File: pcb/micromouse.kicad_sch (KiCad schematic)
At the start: 15 parts, among them J1 AVR-ISP-6, U1 TSSP77038ETR, U2 TSSP77038ETR, U3 TSSP77038ETR, U4 TSSP77038ETR, U5 TSSP77038ETR, U6 TSSP77038ETR, U7 ATmega328PB-A, U8 MX1508, Y1 Crystal

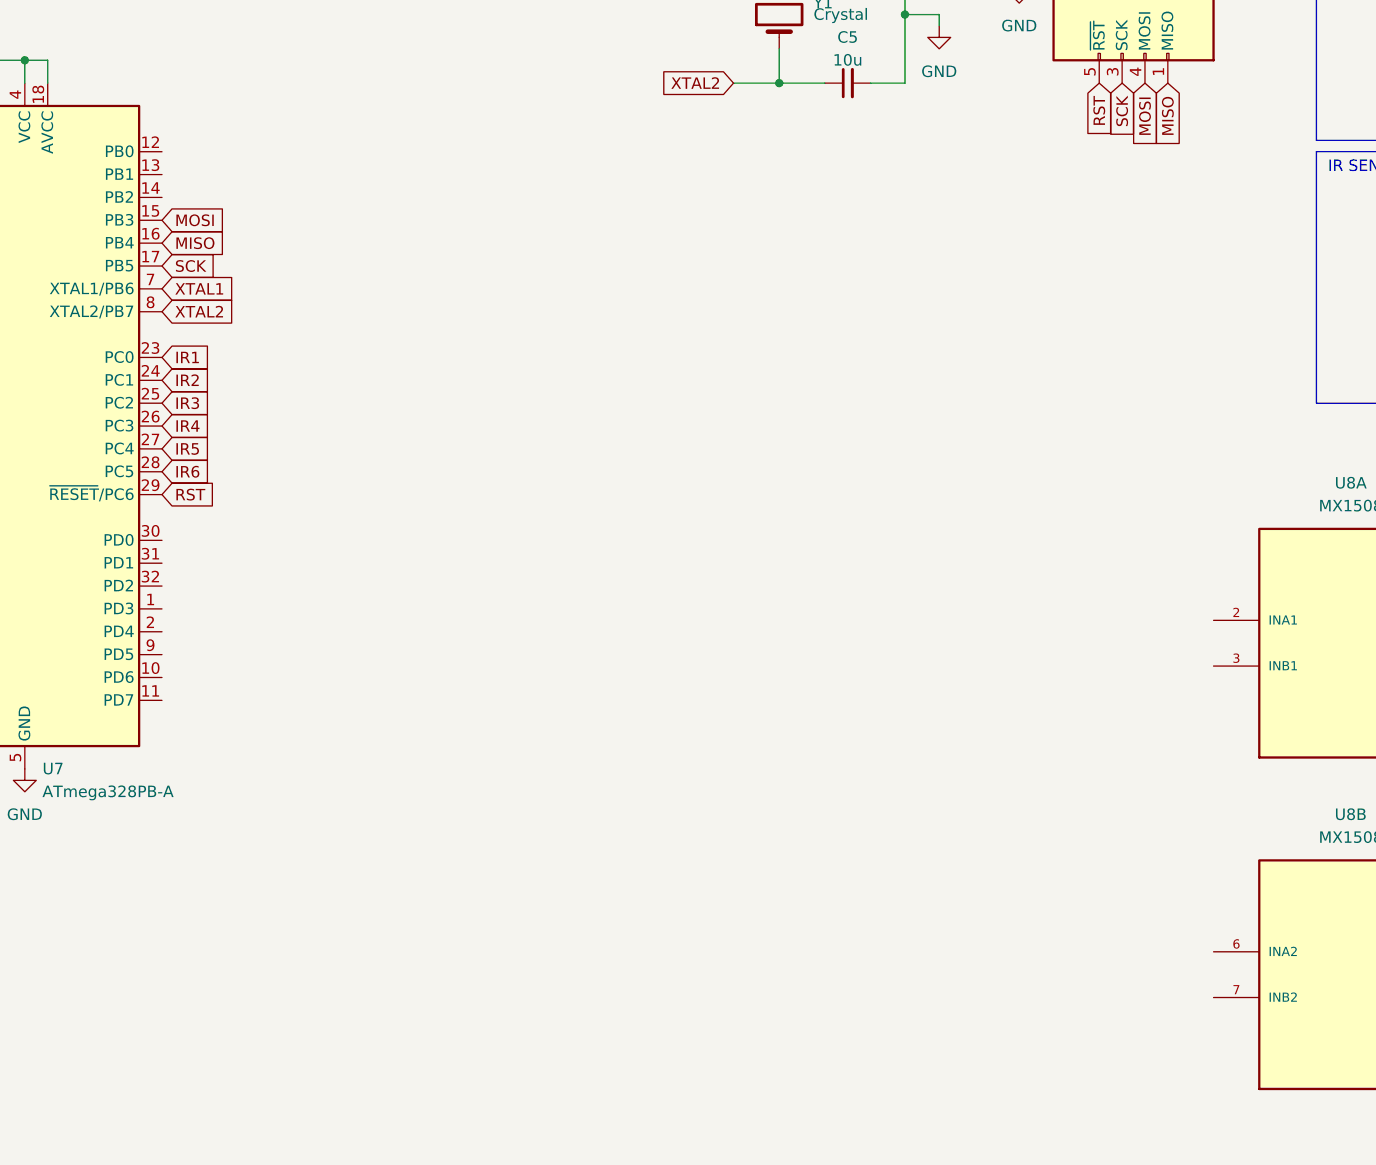
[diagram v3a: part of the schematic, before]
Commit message: add motor control
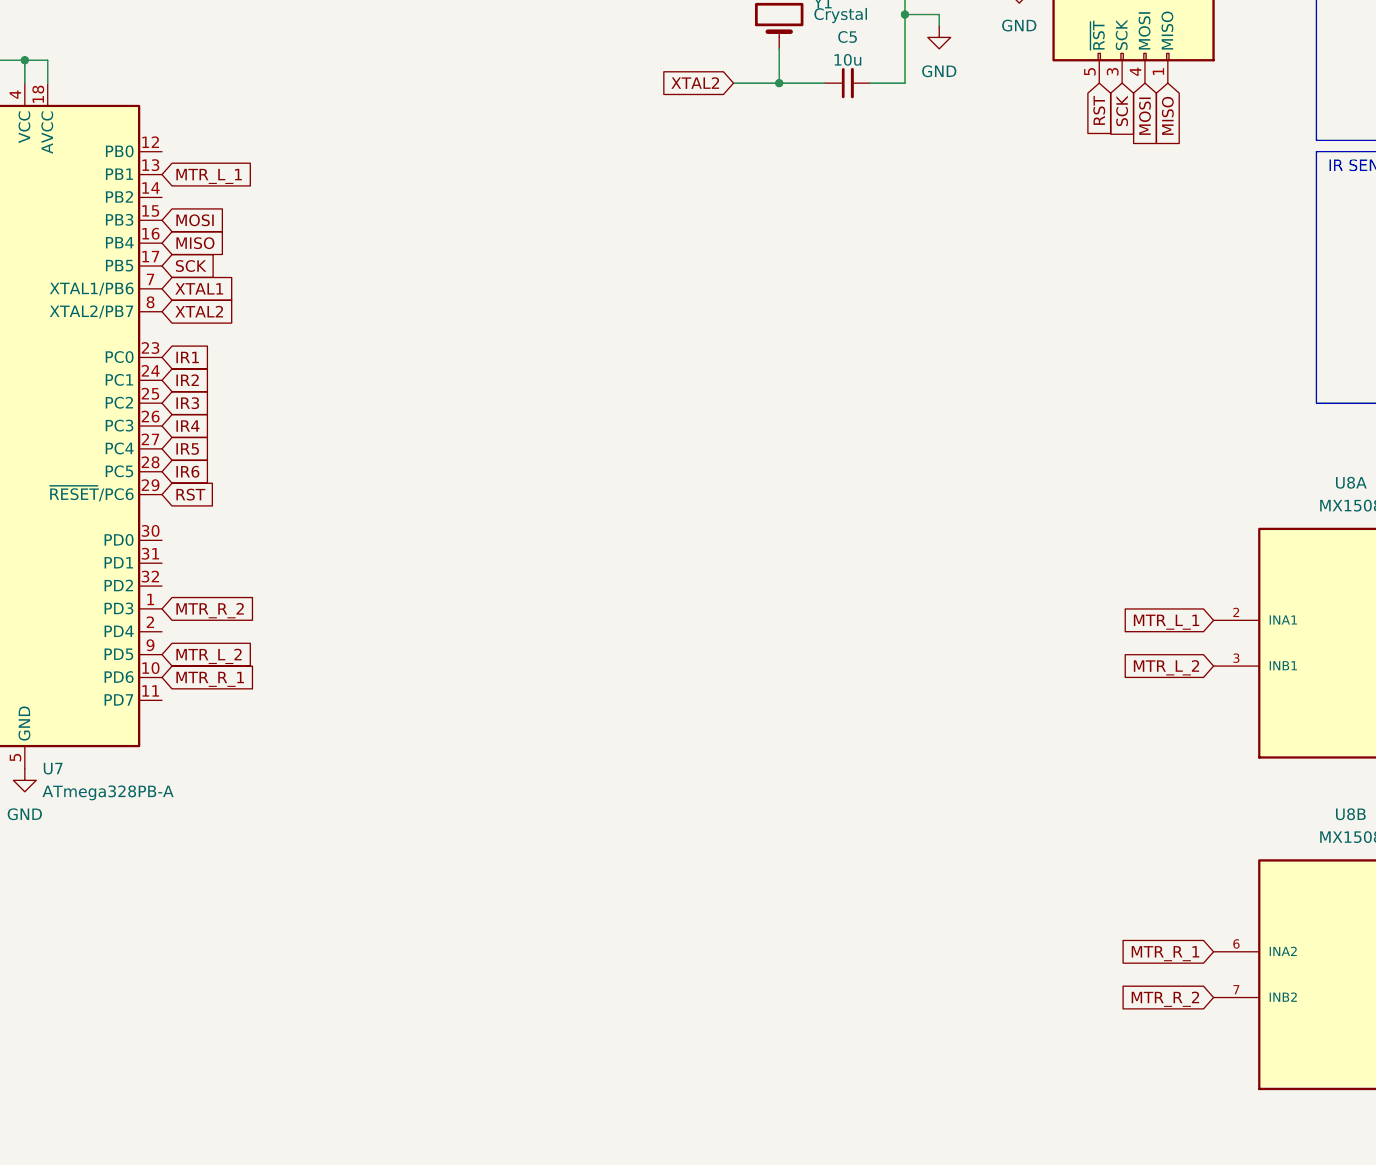
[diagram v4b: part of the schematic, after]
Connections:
- net MTR_R_2: now reaches U7.1 (PD3)
- net MTR_R_2: now also U8.7 (INB2)
- net MTR_R_1: now reaches U7.10 (PD6)
- net MTR_R_1: now also U8.6 (INA2)
- net MTR_L_1: now reaches U7.13 (PB1)
- net MTR_L_1: now also U8.2 (INA1)
- net MTR_L_2: now reaches U7.9 (PD5)
- net MTR_L_2: now also U8.3 (INB1)
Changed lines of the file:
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@@
+    )
+  )
+  (global_label "MTR_R_2" (shape input) (at 71.12 95.25 0) (fields_autoplaced)
+    (effects (font (size 1.27 1.27)) (justify left))
+    (property "Intersheetrefs" "${INTERSHEET_REFS}" (at 82.1295 95.25 0)
+      (effects (font (size 1.27 1.27)) (justify left) hide)
     )
   )
@@
     )
   )
+  (global_label "MTR_R_1" (shape input) (at 187.96 133.35 180) (fields_autoplaced)
+    (effects (font (size 1.27 1.27)) (justify right))
+    (property "Intersheetrefs" "${INTERSHEET_REFS}" (at 176.9505 133.35 0)
+      (effects (font (size 1.27 1.27)) (justify right) hide)
+    )
+  )
   (global_label "MOSI" (shape input) (at 180.34 36.83 270) (fields_autoplaced)
     (effects (font (size 1.27 1.27)) (justify right))
@@
     )
   )
+  (global_label "MTR_L_1" (shape input) (at 187.96 96.52 180) (fields_autoplaced)
+    (effects (font (size 1.27 1.27)) (justify right))
+    (property "Intersheetrefs" "${INTERSHEET_REFS}" (at 177.1924 96.52 0)
+      (effects (font (size 1.27 1.27)) (justify right) hide)
+    )
+  )
   (global_label "IR1" (shape input) (at 274.32 116.84 0) (fields_autoplaced)
     (effects (font (size 1.27 1.27)) (justify left))
@@
     (effects (font (size 1.27 1.27)) (justify left))
     (property "Intersheetrefs" "${INTERSHEET_REFS}" (at 79.5291 62.23 0)
+      (effects (font (size 1.27 1.27)) (justify left) hide)
+    )
+  )
+  (global_label "MTR_R_1" (shape input) (at 71.12 102.87 0) (fields_autoplaced)
+    (effects (font (size 1.27 1.27)) (justify left))
+    (property "Intersheetrefs" "${INTERSHEET_REFS}" (at 82.1295 102.87 0)
       (effects (font (size 1.27 1.27)) (justify left) hide)
     )
@@
     )
   )
+  (global_label "MTR_L_2" (shape input) (at 187.96 101.6 180) (fields_autoplaced)
+    (effects (font (size 1.27 1.27)) (justify right))
+    (property "Intersheetrefs" "${INTERSHEET_REFS}" (at 177.1924 101.6 0)
+      (effects (font (size 1.27 1.27)) (justify right) hide)
+    )
+  )
   (global_label "IR5" (shape input) (at 71.12 77.47 0) (fields_autoplaced)
     (effects (font (size 1.27 1.27)) (justify left))
@@
     (effects (font (size 1.27 1.27)) (justify right))
     (property "Intersheetrefs" "${INTERSHEET_REFS}" (at 177.8 43.4853 90)
+      (effects (font (size 1.27 1.27)) (justify right) hide)
+    )
+  )
+  (global_label "MTR_R_2" (shape input) (at 187.96 138.43 180) (fields_autoplaced)
+    (effects (font (size 1.27 1.27)) (justify right))
+    (property "Intersheetrefs" "${INTERSHEET_REFS}" (at 176.9505 138.43 0)
       (effects (font (size 1.27 1.27)) (justify right) hide)
     )
@@
     )
   )
+  (global_label "MTR_L_1" (shape input) (at 71.12 46.99 0) (fields_autoplaced)
+    (effects (font (size 1.27 1.27)) (justify left))
+    (property "Intersheetrefs" "${INTERSHEET_REFS}" (at 81.8876 46.99 0)
+      (effects (font (size 1.27 1.27)) (justify left) hide)
+    )
+  )
   (global_label "IR4" (shape input) (at 274.32 29.21 0) (fields_autoplaced)
     (effects (font (size 1.27 1.27)) (justify left))
@@
       (effects (font (size 1.27 1.27)) (justify left) hide)
     )
+  )
+  (global_label "MTR_L_2" (shape input) (at 71.12 100.33 0) (fields_autoplaced)
+    (effects (font (size 1.27 1.27)) (justify left))
+    (property "Intersheetrefs" "${INTERSHEET_REFS}" (at 81.8876 100.33 0)
+      (effects (font (size 1.27 1.27)) (justify left) hide)
+    )

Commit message: wiring mcu
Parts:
- C1, C2, C3, C4, C5: footprint (none) -> Capacitor_SMD:C_0603_1608Metric
- J1: footprint (none) -> Connector_IDC:IDC-Header_2x03_P2.54mm_Horizontal
- U1, U2, U3, U4, U5, U6: footprint TSSP77038ETR:TSSP770 -> Library:TSSP77
- Y1: footprint (none) -> Crystal:Crystal_SMD_HC49-SD
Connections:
- net +3.3V: now also U1.2 (VS), U2.2 (VS), U3.2 (VS), U4.2 (VS), U5.2 (VS), U6.2 (VS); no longer U1.P$2 (VS), U2.P$2 (VS), U3.P$2 (VS), U4.P$2 (VS), U5.P$2 (VS), U6.P$2 (VS)
- net GND: now also U1.1 (GND), U1.4 (GND1), U2.1 (GND), U2.4 (GND1), U3.1 (GND), U3.4 (GND1), U4.1 (GND), U4.4 (GND1), U5.1 (GND), U5.4 (GND1), U6.1 (GND), U6.4 (GND1); no longer U1.P$1 (GND), U1.P$4 (GND1), U2.P$1 (GND), U2.P$4 (GND1), U3.P$1 (GND), U3.P$4 (GND1), U4.P$1 (GND), U4.P$4 (GND1), U5.P$1 (GND), U5.P$4 (GND1), U6.P$1 (GND), U6.P$4 (GND1)
- net IR1: now also U1.3 (OUT); no longer U1.P$3 (OUT)
- net IR2: now also U2.3 (OUT); no longer U2.P$3 (OUT)
- net IR3: now also U3.3 (OUT); no longer U3.P$3 (OUT)
- net IR4: now also U4.3 (OUT); no longer U4.P$3 (OUT)
- net IR5: now also U5.3 (OUT); no longer U5.P$3 (OUT)
- net IR6: now also U6.3 (OUT); no longer U6.P$3 (OUT)
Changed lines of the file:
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@@
       (effects (font (size 1.27 1.27)))
     )
-    (property "Footprint" "TSSP77038ETR:TSSP770" (at 224.79 58.42 0)
+    (property "Footprint" "Library:TSSP77" (at 224.79 58.42 0)
       (effects (font (size 1.27 1.27)) (justify bottom) hide)
     )
@@
       (effects (font (size 1.27 1.27)) (justify bottom) hide)
     )
-    (pin "P$1")
-    (pin "P$2")
-    (pin "P$3")
-    (pin "P$4")
+    (pin "1")
+    (pin "2")
+    (pin "3")
+    (pin "4")
     (instances
       (project "micromouse"
@@
       (effects (font (size 1.27 1.27)))
     )
-    (property "Footprint" "" (at 147.32 36.83 0)
+    (property "Footprint" "Capacitor_SMD:C_0603_1608Metric" (at 147.32 36.83 0)
       (effects (font (size 1.27 1.27)) hide)
     )
@@
       (effects (font (size 1.27 1.27)) (justify left))
     )
-    (property "Footprint" "" (at 35.56 38.1 0)
+    (property "Footprint" "Capacitor_SMD:C_0603_1608Metric" (at 35.56 38.1 0)
       (effects (font (size 1.27 1.27)) hide)
     )
@@
       (effects (font (size 1.27 1.27)) (justify left))
     )
-    (property "Footprint" "" (at 27.94 38.1 0)
+    (property "Footprint" "Capacitor_SMD:C_0603_1608Metric" (at 27.94 38.1 0)
       (effects (font (size 1.27 1.27)) hide)
     )
@@
       (effects (font (size 1.27 1.27)))
     )
-    (property "Footprint" "" (at 179.07 20.32 90)
+    (property "Footprint" "Connector_IDC:IDC-Header_2x03_P2.54mm_Horizontal" (at 179.07 20.32 90)
       (effects (font (size 1.27 1.27)) hide)
     )
@@
       (effects (font (size 1.27 1.27)))
     )
-    (property "Footprint" "TSSP77038ETR:TSSP770" (at 266.7 116.84 0)
+    (property "Footprint" "Library:TSSP77" (at 266.7 116.84 0)
       (effects (font (size 1.27 1.27)) (justify bottom) hide)
     )
@@
       (effects (font (size 1.27 1.27)) (justify bottom) hide)
     )
-    (pin "P$1")
-    (pin "P$2")
-    (pin "P$3")
-    (pin "P$4")
+    (pin "1")
+    (pin "2")
+    (pin "3")
+    (pin "4")
     (instances
       (project "micromouse"
@@
       (effects (font (size 1.27 1.27)) (justify left))
     )
-    (property "Footprint" "" (at 20.32 38.1 0)
+    (property "Footprint" "Capacitor_SMD:C_0603_1608Metric" (at 20.32 38.1 0)
       (effects (font (size 1.27 1.27)) hide)
     )
@@
       (effects (font (size 1.27 1.27)))
     )
-    (property "Footprint" "TSSP77038ETR:TSSP770" (at 266.7 58.42 0)
+    (property "Footprint" "Library:TSSP77" (at 266.7 58.42 0)
       (effects (font (size 1.27 1.27)) (justify bottom) hide)
     )
@@
       (effects (font (size 1.27 1.27)) (justify bottom) hide)
     )
-    (pin "P$1")
-    (pin "P$2")
-    (pin "P$3")
-    (pin "P$4")
+    (pin "1")
+    (pin "2")
+    (pin "3")
+    (pin "4")
     (instances
       (project "micromouse"
@@
       (effects (font (size 1.27 1.27)))
     )
-    (property "Footprint" "TSSP77038ETR:TSSP770" (at 266.7 29.21 0)
+    (property "Footprint" "Library:TSSP77" (at 266.7 29.21 0)
       (effects (font (size 1.27 1.27)) (justify bottom) hide)
     )
@@
       (effects (font (size 1.27 1.27)) (justify bottom) hide)
     )
-    (pin "P$1")
-    (pin "P$2")
-    (pin "P$3")
-    (pin "P$4")
+    (pin "1")
+    (pin "2")
+    (pin "3")
+    (pin "4")
     (instances
       (project "micromouse"
@@
       (effects (font (size 1.27 1.27)))
     )
-    (property "Footprint" "TSSP77038ETR:TSSP770" (at 266.7 87.63 0)
+    (property "Footprint" "Library:TSSP77" (at 266.7 87.63 0)
       (effects (font (size 1.27 1.27)) (justify bottom) hide)
     )
@@
       (effects (font (size 1.27 1.27)) (justify bottom) hide)
     )
-    (pin "P$1")
-    (pin "P$2")
-    (pin "P$3")
-    (pin "P$4")
+    (pin "1")
+    (pin "2")
+    (pin "3")
+    (pin "4")
     (instances
       (project "micromouse"
@@
       (effects (font (size 1.27 1.27)))
     )
-    (property "Footprint" "TSSP77038ETR:TSSP770" (at 224.79 29.21 0)
+    (property "Footprint" "Library:TSSP77" (at 224.79 29.21 0)
       (effects (font (size 1.27 1.27)) (justify bottom) hide)
     )
@@
       (effects (font (size 1.27 1.27)) (justify bottom) hide)
     )
-    (pin "P$1")
-    (pin "P$2")
-    (pin "P$3")
-    (pin "P$4")
+    (pin "1")
+    (pin "2")
+    (pin "3")
+    (pin "4")
     (instances
       (project "micromouse"
@@
       (effects (font (size 1.27 1.27)) (justify right))
     )
-    (property "Footprint" "" (at 139.7 29.21 0)
+    (property "Footprint" "Crystal:Crystal_SMD_HC49-SD" (at 139.7 29.21 0)
       (effects (font (size 1.27 1.27)) hide)
     )
@@
       (effects (font (size 1.27 1.27)))
     )
-    (property "Footprint" "" (at 147.32 22.86 0)
-      (effects (font (size 1.27 1.27)) hide)
-    )
+    (property "Footprint" "Capacitor_SMD:C_0603_1608Metric" (at 147.32 22.86 0)
+      (effects (font (size 1.27 1.27)) hide)
+    )
